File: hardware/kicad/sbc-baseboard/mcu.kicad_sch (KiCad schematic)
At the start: 36 parts, among them J16 SWD, J3 USB-C HID to target, SW201 RESET, U201 MK64FN1M0VLL12, U202 USBLC6-2SC6, Y201 32.768kHz

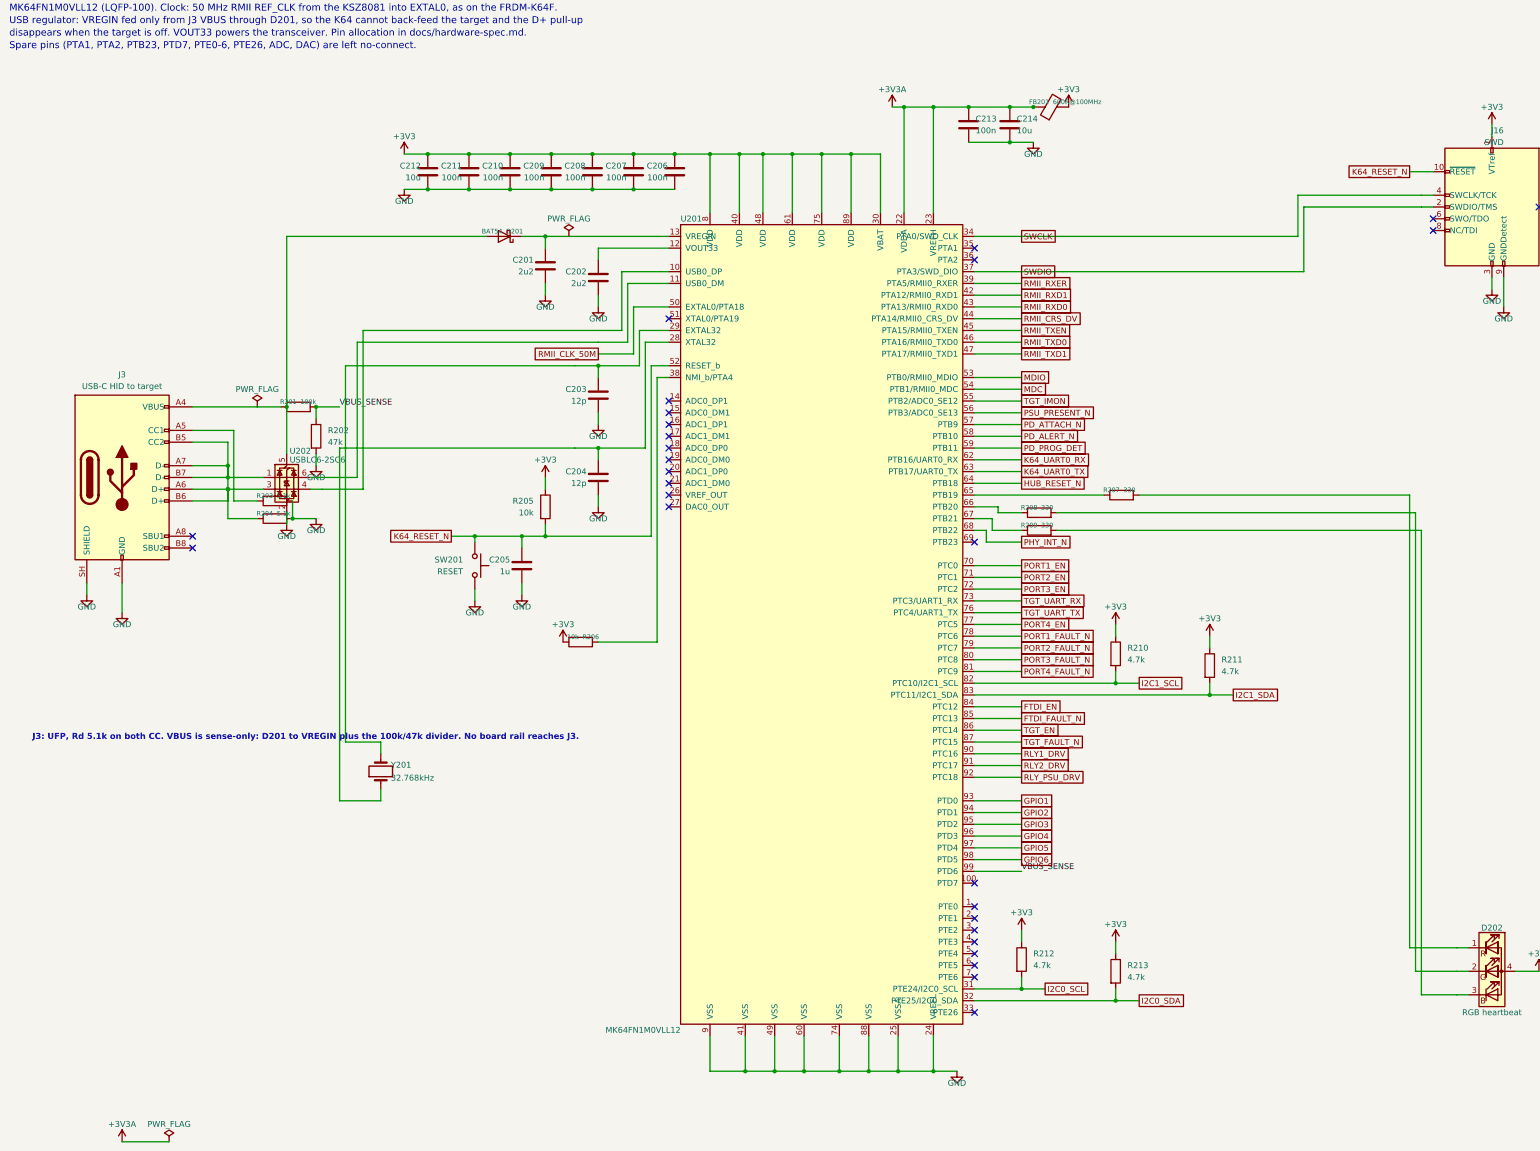
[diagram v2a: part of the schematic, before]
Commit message: Placement pass: every sheet clean on all four layout gates
Hanging parts now sit with their near pin between rows, so a pull-up on
the next lane crosses only its lead; parts slide past a neighbour's parts
and text, not its plain wire, and never let a wire run through a body or
a rail symbol. Chains on top/bottom pins run sideways first. Route
channels are numbered per route. Power symbols that would land on a
neighbouring wire get a jog or a hook. The VBUS sense divider moved to
the K64's ADC pin so J3's VBUS lane is a short stretch the ESD array taps;
the J1 tap sits before its divider. Relay coil clusters are drawn by the
engine. Port switches moved so OUT stays on the VBUS row.

ERC 0, no endpoint contacts, no merged rails, no wires through bodies,
no inverted power symbols, on all eight sheets; netlist equivalent to the
first pass (331 parts, 354 nets); USB D+/D-, VBUS and I2C paths verified
pin by pin.

Co-Authored-By: Claude Fable 5.1 <noreply@anthropic.com>
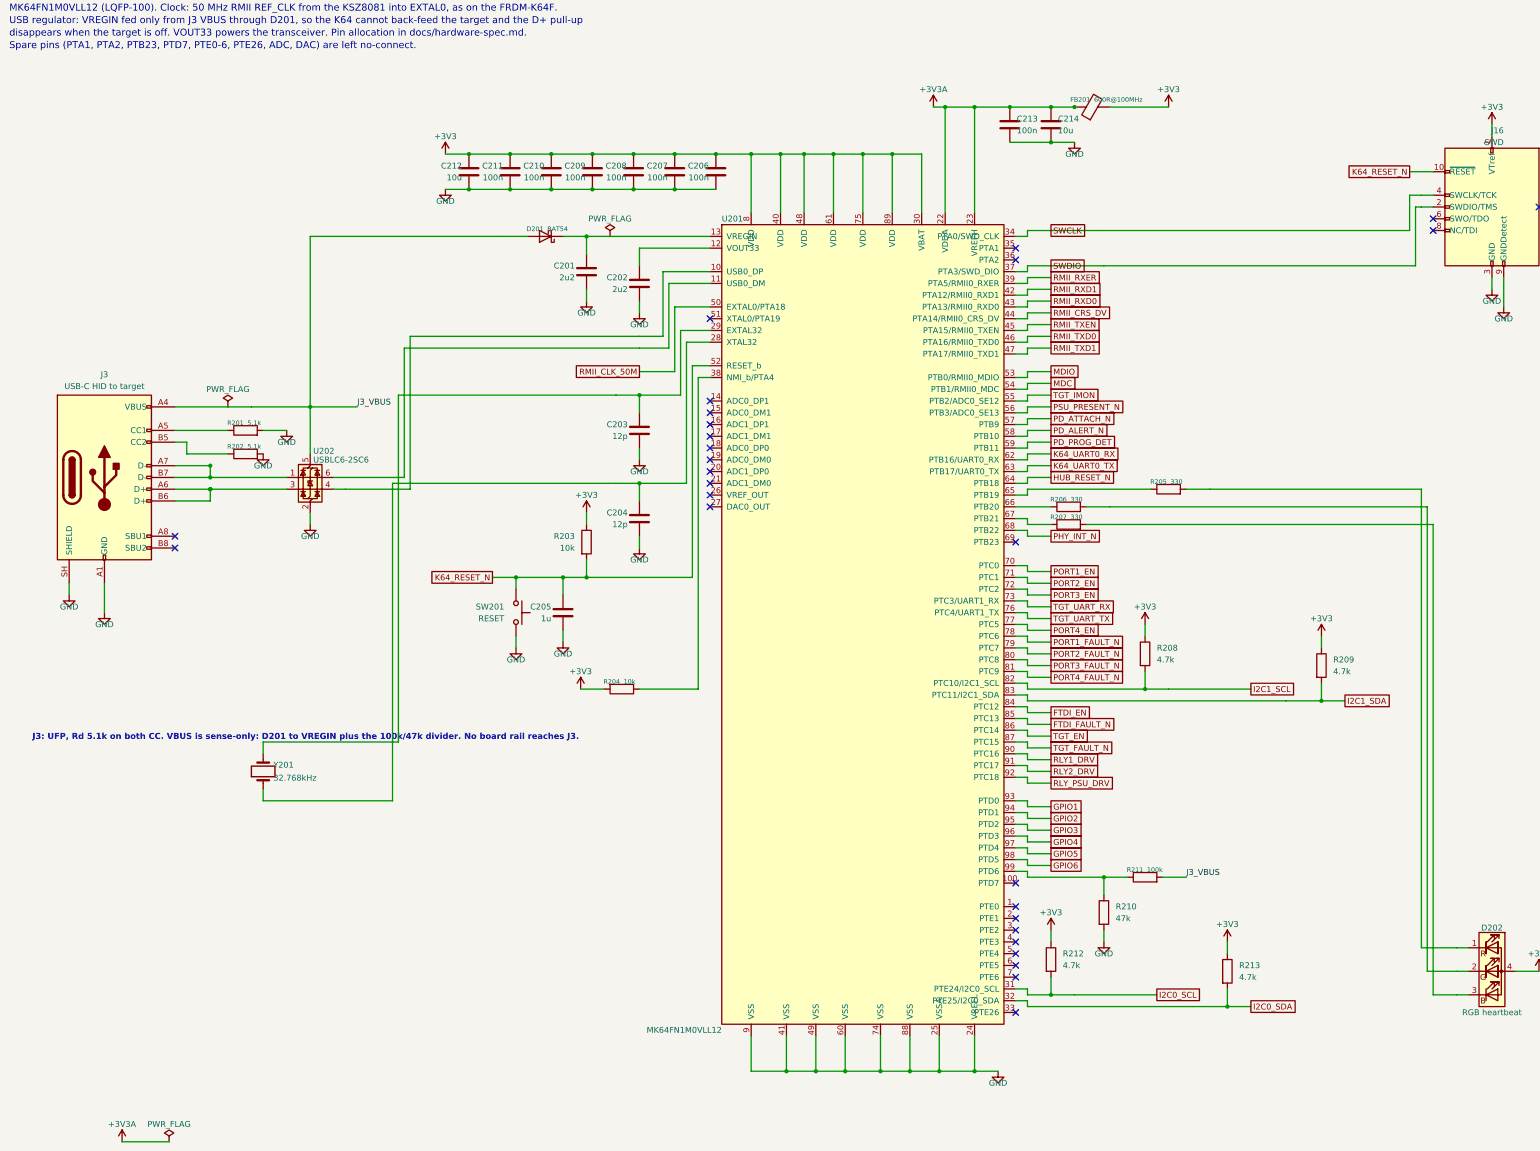
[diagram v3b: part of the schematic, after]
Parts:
- R201: value 100k -> 5.1k
- R202: value 47k -> 5.1k
- R203, R204: value 5.1k -> 10k
- R205, R206: value 10k -> 330
- R208, R209: value 330 -> 4.7k
- R210: value 4.7k -> 47k
- R211: value 4.7k -> 100k
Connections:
- net +3V3: now also R203.1, R204.2, R208.1, R209.1; no longer R205.1, R206.2, R210.1, R211.1
- net GND: now also R201.2, R210.2; no longer R203.2, R204.2
- net I2C1_SCL: now also R208.2; no longer R210.2
- net I2C1_SDA: now also R209.2; no longer R211.2
- net K64_RESET_N: now also R203.2; no longer R205.2
- net at U201.67 (PTB21): now also R207.1; no longer R209.1
- net at D202.3 (BK): now also R207.2; no longer R209.2
- net J3_VBUS: now reaches J3.A4 (VBUS), J3.A9 (VBUS), J3.B4 (VBUS), J3.B9 (VBUS)
- net J3_VBUS: now also D201.2 (A), R211.2, U202.5 (VBUS); no longer R201.1
- net at U201.65 (PTB19): now also R205.1; no longer R207.1
- net at D202.1 (RK): now also R205.2; no longer R207.2
- net at U201.38 (NMI_b/PTA4): now also R204.1; no longer R206.1
- net at U201.66 (PTB20): now also R206.1; no longer R208.1
- net at J3.A5 (CC1): now also R201.1; no longer R203.1
- net at D202.2 (GK): now also R206.2; no longer R208.2
- removed net VBUS_SENSE: R201.2, R202.1, U201.99 (PTD6)
- new net: J3.A7 (D-), J3.B7 (D-), U202.1 (I/O1)
- new net: J3.A6 (D+), J3.B6 (D+), U202.3 (I/O2)
- new net: R210.1, R211.1, U201.99 (PTD6)
- new net: J3.B5 (CC2), R202.1

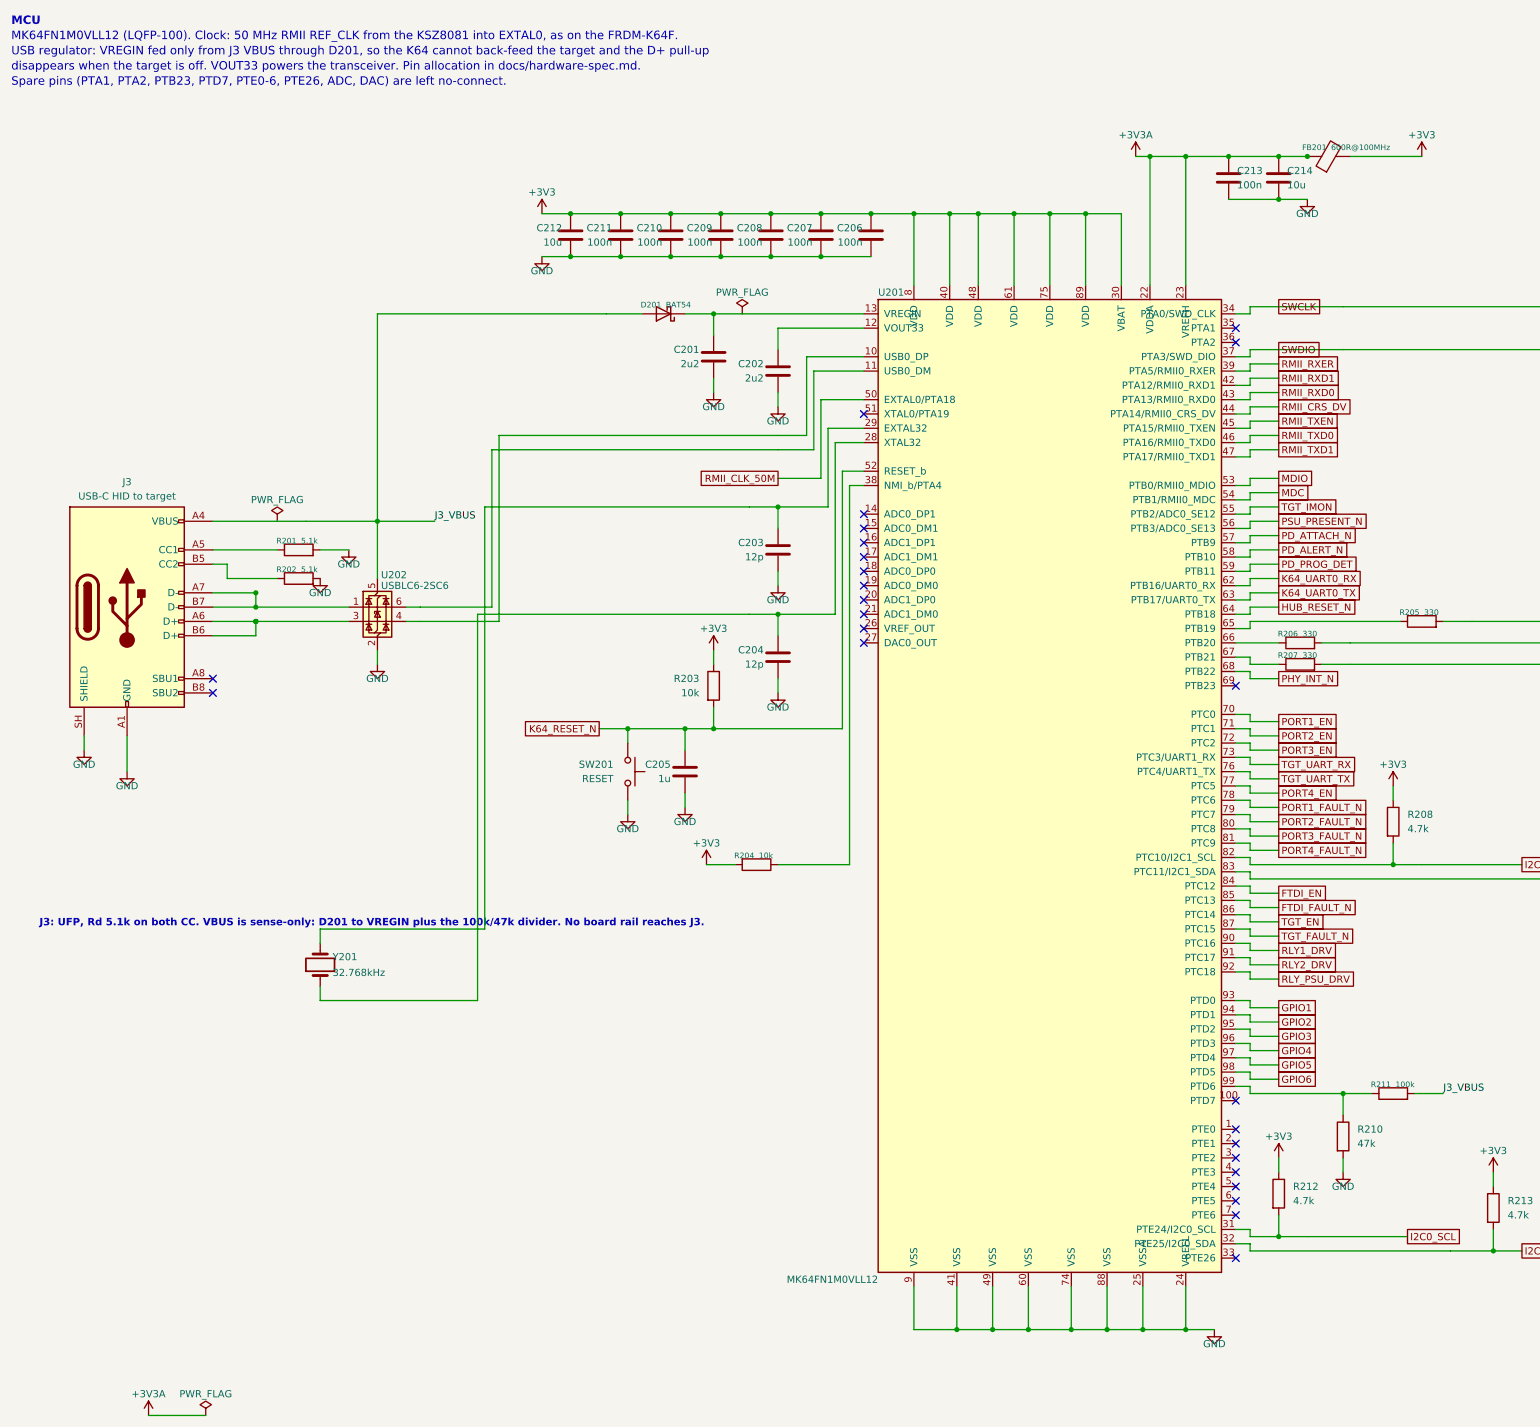
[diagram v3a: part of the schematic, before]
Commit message: Symbol name clearance, divider at the reading pin, inlet TVS orientation
Symbols: a top or bottom pin's name runs vertically into the body, so box
symbols now grow outward by whole rows wherever such a name would reach a
side pin's name (USB2517 three rows on top, K64 two rows top and bottom,
PCA9517A three rows on top); the side-pin rows stay where they were so the
sheet layouts are unaffected. U402's VDD names no longer print over USBUP_DP.

Frame pass: nothing on the sheet frame or the title block, enforced by the
layout gate (usable area 15..405 x 15..282 mm, title block from 300/253).

Flow pass: pull-ups hang up to their rail, pull-downs hang down (R408/R409
and the other strap and sense resistors). The J1 VBUS_DET divider sits at
U402 pin 44, the pin that reads it; J1's VBUS lane is a plain stretch that
U401 taps; J1 and U401 lifted clear of the hub's +3V3 bus. The hub's left
strap lanes turn in columns starting at x = 118.11 so they clear the bottom
decoupling ladders (fan() grew a turn_at argument for this).

Inlet TVS D102 hangs from J2's VBUS lane as a D_Zener with its cathode on
VBUS_IN. At 8579cd2 it was drawn with the bidirectional D_TVS symbol and
pad 1 (the SMA cathode) on GND, which would have forward-biased it.

Bucks: the FB pulls start past the catch diode's text; the two notes are
rewrapped and sit between U101 and the compensation parts.

Gates on every sheet: ERC 0, endpoint contacts 0, rail merges 0, frame 0,
no text on bodies or wires. Connectivity identical to 8579cd2 (symmetric
passives order-free) except the TVS orientation.

Co-Authored-By: Claude Fable 5.1 <noreply@anthropic.com>
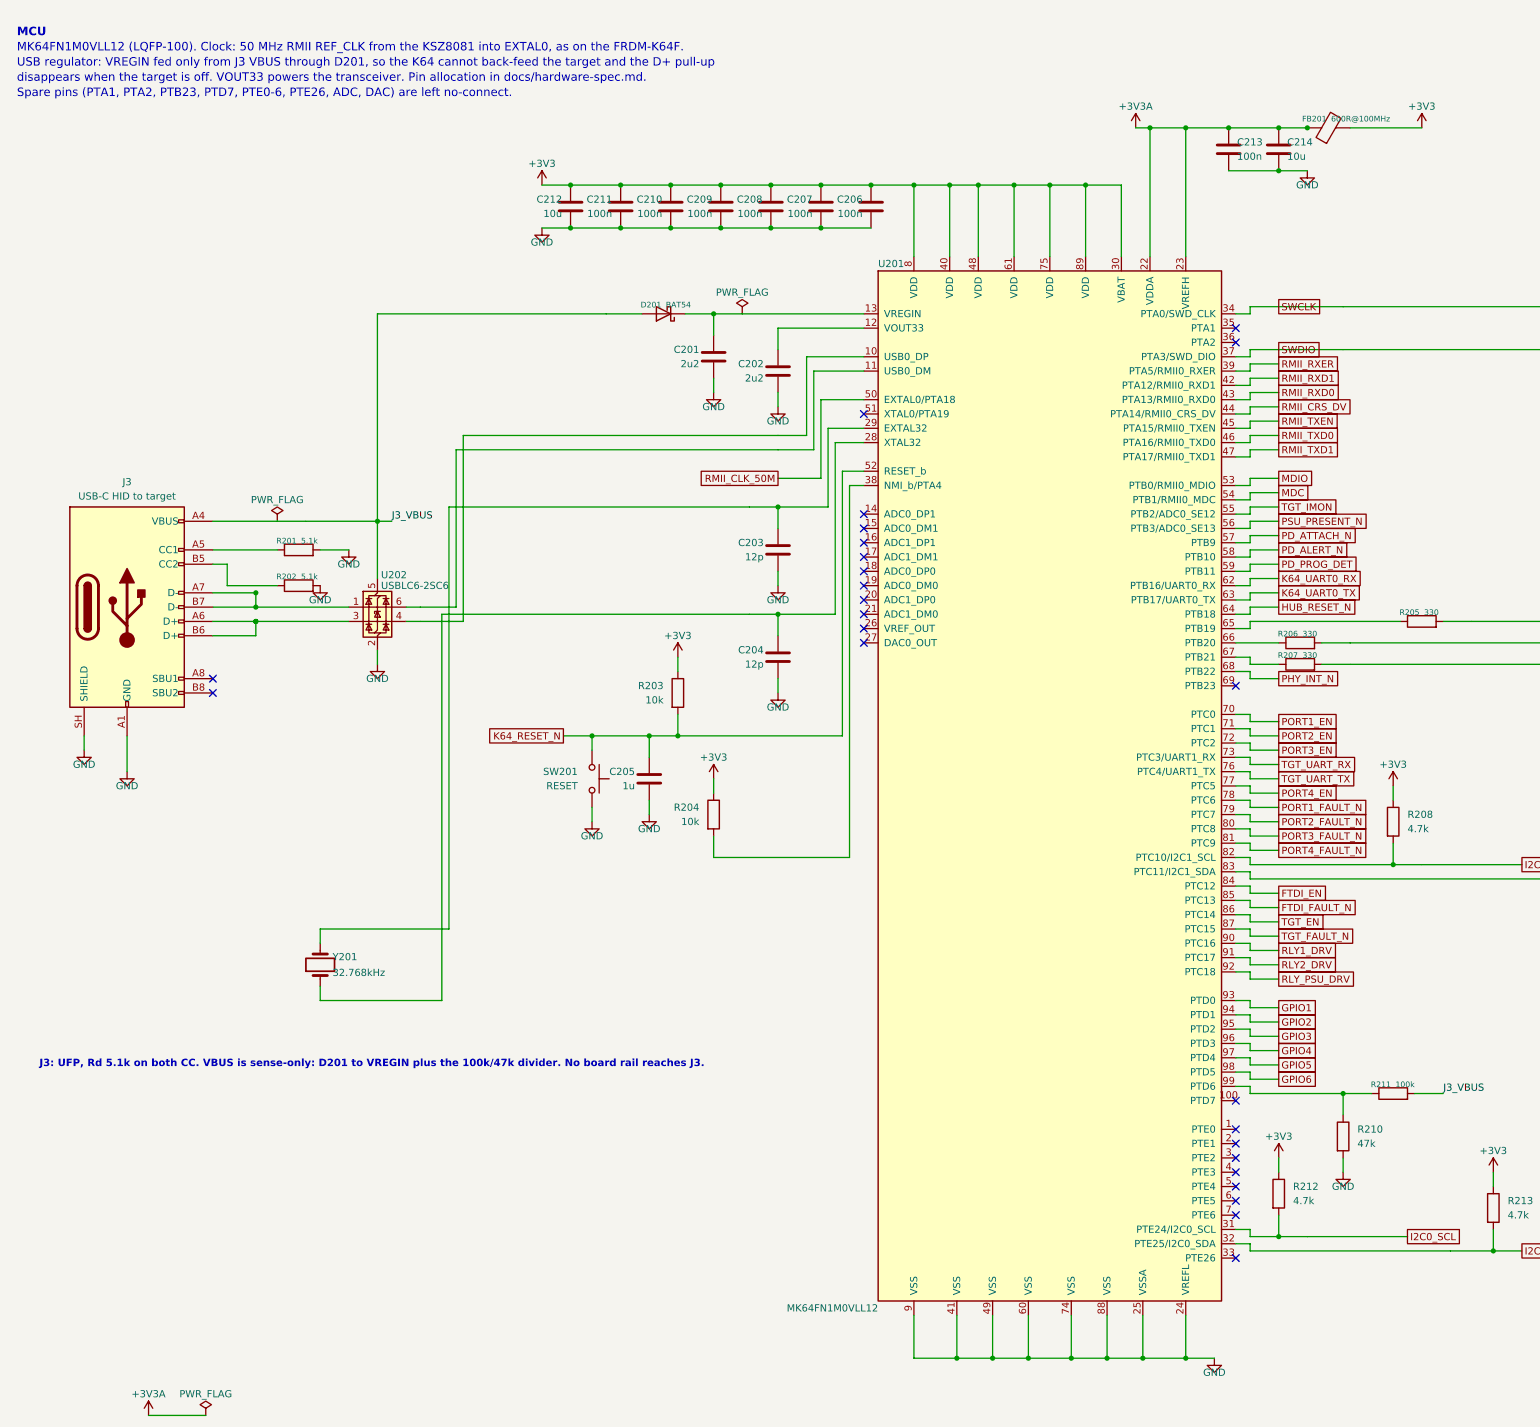
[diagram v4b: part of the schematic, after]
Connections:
- net +3V3: now also R204.1; no longer R204.2
- net at U201.38 (NMI_b/PTA4): now also R204.2; no longer R204.1
